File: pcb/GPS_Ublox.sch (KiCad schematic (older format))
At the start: 0 parts

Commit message: Add MTX2 circuit and add a sheet for power supply/regulation
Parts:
- added IC?: u-blox_CAM-M8Q, symbol u-blox_CAM-M8Q
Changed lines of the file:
@@
 LIBS:max-7q
 LIBS:ms5611-01ba03
-LIBS:quarter_wave_ant
 LIBS:resistor
 LIBS:rfm69w
-LIBS:sma
 LIBS:stm32f405vgt
 LIBS:swd
@@
 LIBS:stm32f072cbt6
 LIBS:jsta
+LIBS:sma
+LIBS:cga0402mlc-12g
 LIBS:woodchuck-cache
 EELAYER 25 0
@@
 $Descr A4 11693 8268
 encoding utf-8
-Sheet 1 6
+Sheet 2 7
 Title ""
 Date ""
@@
 Comment4 ""
 $EndDescr
+$Comp
+L u-blox_CAM-M8Q IC?
+U 1 1 565D0659
+P 5350 2900
+F 0 "IC?" H 4900 3450 60  0000 C CNN
+F 1 "u-blox_CAM-M8Q" H 5250 1400 60  0000 C CNN
+F 2 "" H 5550 2000 60  0000 C CNN
+F 3 "" H 5550 2000 60  0000 C CNN
+	1    5350 2900
+	1    0    0    -1
+$EndComp
 $EndSCHEMATC

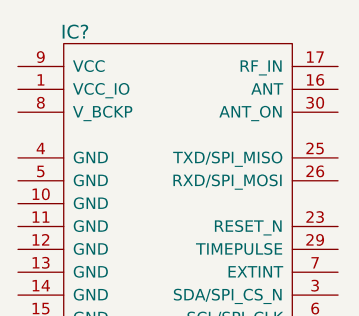
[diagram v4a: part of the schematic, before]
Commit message: Modify pin assignments of MCU
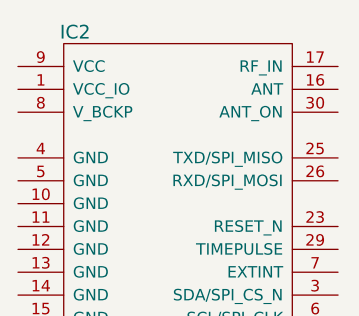
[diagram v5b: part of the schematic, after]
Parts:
- gave numbers to parts that had none: 1
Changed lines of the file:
@@
 $EndDescr
 $Comp
-L u-blox_CAM-M8Q IC?
+L u-blox_CAM-M8Q IC2
 U 1 1 565D0659
 P 5350 2900
-F 0 "IC?" H 4900 3450 60  0000 C CNN
+F 0 "IC2" H 4900 3450 60  0000 C CNN
 F 1 "u-blox_CAM-M8Q" H 5250 1400 60  0000 C CNN
 F 2 "" H 5550 2000 60  0000 C CNN

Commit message: Begin routing GPS
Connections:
- net +3V3: now reaches IC2.1 (VCC_IO)
- net +3V3: now also IC2.9 (VCC)
- net GND: now reaches IC2.10 (GND)
- net GND: now also IC2.11 (GND), IC2.12 (GND), IC2.13 (GND), IC2.14 (GND), IC2.15 (GND), IC2.18 (GND), IC2.19 (GND), IC2.21 (GND), IC2.22 (GND), IC2.27 (GND), IC2.31 (GND), IC2.4 (GND), IC2.5 (GND)
- no-connect marks 0 -> 1
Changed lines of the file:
@@
 	1    0    0    -1
 $EndComp
+$Comp
+L GND #PWR?
+U 1 1 56AAB217
+P 4550 4300
+F 0 "#PWR?" H 4550 4050 50  0001 C CNN
+F 1 "GND" H 4550 4150 50  0000 C CNN
+F 2 "" H 4550 4300 60  0000 C CNN
+F 3 "" H 4550 4300 60  0000 C CNN
+	1    4550 4300
+	1    0    0    -1
+$EndComp
+Wire Wire Line
+	4650 4200 4550 4200
+Wire Wire Line
+	4550 2900 4550 4300
+Wire Wire Line
+	4650 2900 4550 2900
+Connection ~ 4550 4200
+Wire Wire Line
+	4650 3000 4550 3000
+Connection ~ 4550 3000
+Wire Wire Line
+	4650 3100 4550 3100
+Connection ~ 4550 3100
+Wire Wire Line
+	4650 3200 4550 3200
+Connection ~ 4550 3200
+Wire Wire Line
+	4650 3300 4550 3300
+Connection ~ 4550 3300
+Wire Wire Line
+	4650 3400 4550 3400
+Connection ~ 4550 3400
+Wire Wire Line
+	4650 3500 4550 3500
+Connection ~ 4550 3500
+Wire Wire Line
+	4650 3600 4550 3600
+Connection ~ 4550 3600
+Wire Wire Line
+	4650 3700 4550 3700
+Connection ~ 4550 3700
+Wire Wire Line
+	4650 3800 4550 3800
+Connection ~ 4550 3800
+Wire Wire Line
+	4650 3900 4550 3900
+Connection ~ 4550 3900
+Wire Wire Line
+	4650 4000 4550 4000
+Connection ~ 4550 4000
+Wire Wire Line
+	4650 4100 4550 4100
+Connection ~ 4550 4100
+$Comp
+L +3.3V #PWR?
+U 1 1 56AAB35F
+P 4550 2400
+F 0 "#PWR?" H 4550 2250 50  0001 C CNN
+F 1 "+3.3V" H 4550 2540 50  0000 C CNN
+F 2 "" H 4550 2400 60  0000 C CNN
+F 3 "" H 4550 2400 60  0000 C CNN
+	1    4550 2400
+	1    0    0    -1
+$EndComp
+Wire Wire Line
+	4550 2400 4550 2600
+Wire Wire Line
+	4550 2500 4650 2500
+Wire Wire Line
+	4550 2600 4650 2600
+Connection ~ 4550 2500
+NoConn ~ 4650 2700
+Text HLabel 7650 2800 0    60   Input ~ 0
+GPS_FROM_MCU
+Text HLabel 7700 3000 0    60   Output ~ 0
+GPS_TO_MCU
 $EndSCHEMATC

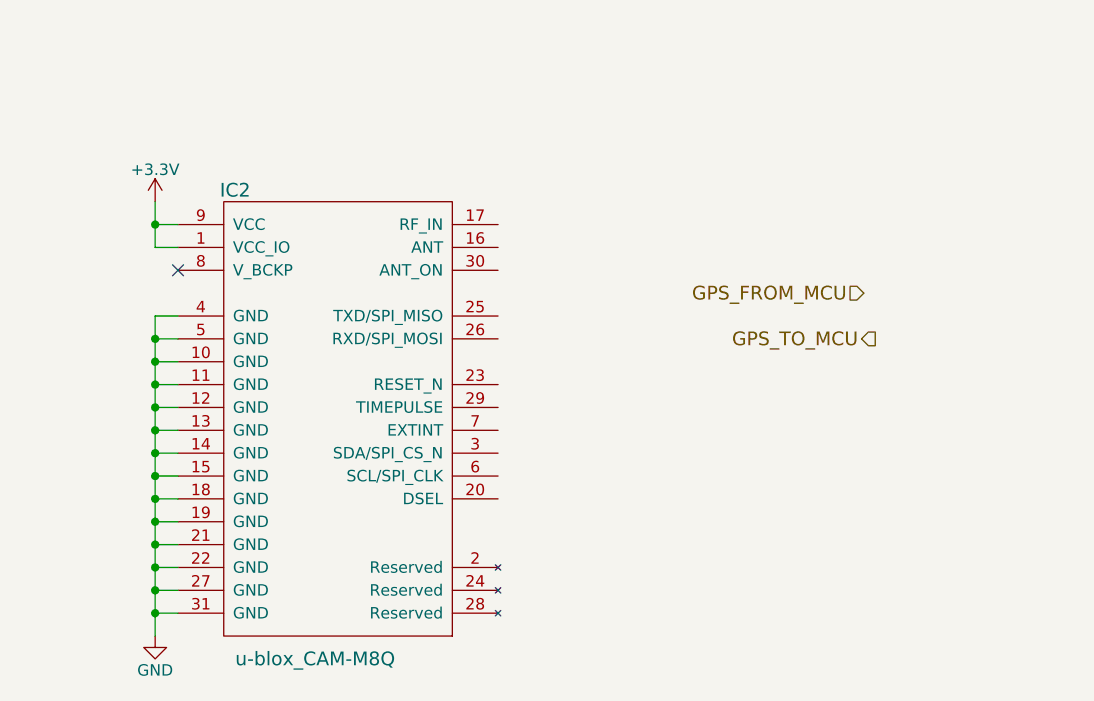
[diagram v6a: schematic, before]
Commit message: Finished schematics for GPS. TODO: check DSEL, and that RX TX are connected correctly. Make sure capacitor and resistor values are ok.
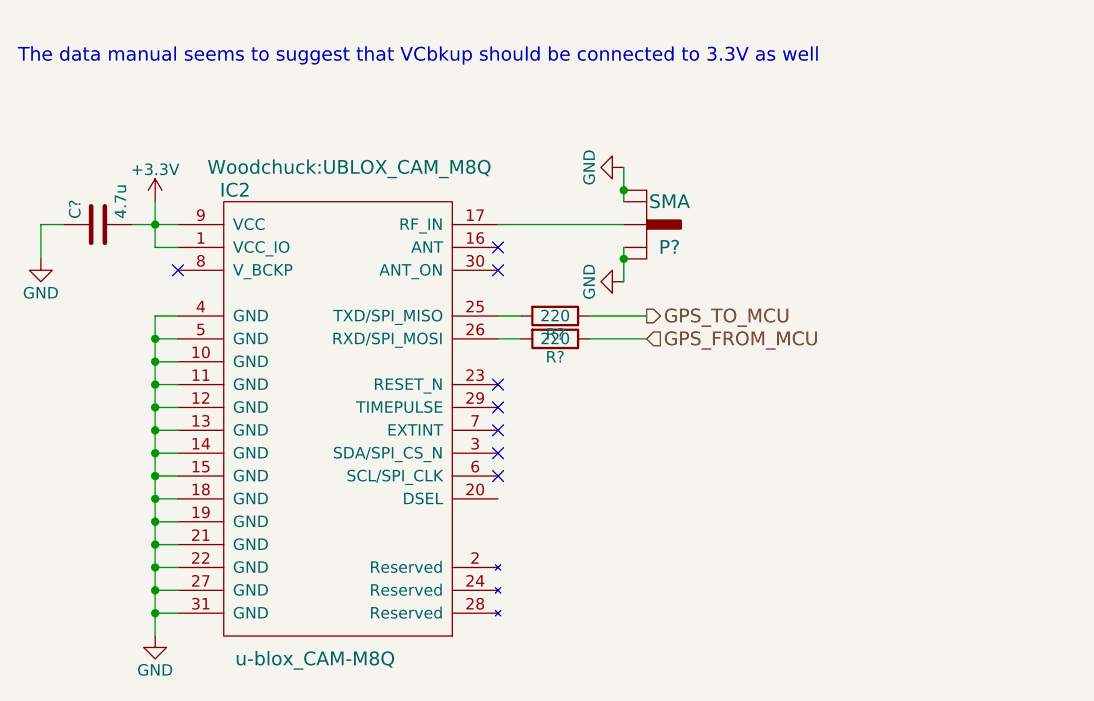
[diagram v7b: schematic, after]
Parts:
- added C?: 4.7u, symbol C
- added P?: SMA, symbol SMA
- added R? (x2): 220, symbol R
- IC2: footprint (none) -> Woodchuck:UBLOX_CAM_M8Q
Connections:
- net +3V3: now also C?.2
- net GND: now also C?.1, P?.2 (GND), P?.3 (GND), P?.4 (GND), P?.5 (GND)
- net GPS_FROM_MCU: now also R?.1
- net GPS_TO_MCU: now also R?.1
- net at IC2.17 (RF_IN): now also P?.1 (RF)
- net at IC2.25 (TXD/SPI_MISO): now also R?.2
- net at IC2.26 (RXD/SPI_MOSI): now also R?.2
- no-connect marks 1 -> 8
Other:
- note added: "The data manual seems to suggest that VCbkup should be connected to 3.3V as well"
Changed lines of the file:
@@
 F 0 "IC2" H 4900 3450 60  0000 C CNN
 F 1 "u-blox_CAM-M8Q" H 5250 1400 60  0000 C CNN
-F 2 "" H 5550 2000 60  0000 C CNN
+F 2 "Woodchuck:UBLOX_CAM_M8Q" H 5400 3550 60  0000 C CNN
 F 3 "" H 5550 2000 60  0000 C CNN
 	1    5350 2900
@@
 	4550 2400 4550 2600
 Wire Wire Line
-	4550 2500 4650 2500
+	4450 2500 4650 2500
 Wire Wire Line
 	4550 2600 4650 2600
 Connection ~ 4550 2500
 NoConn ~ 4650 2700
-Text HLabel 7650 2800 0    60   Input ~ 0
+Text HLabel 6700 3000 2    60   Input ~ 0
 GPS_FROM_MCU
-Text HLabel 7700 3000 0    60   Output ~ 0
+Text HLabel 6700 2900 2    60   Output ~ 0
 GPS_TO_MCU
+Text Notes 3950 1800 0    60   ~ 0
+The data manual seems to suggest that VCbkup should be connected to 3.3V as well
+$Comp
+L C C?
+U 1 1 56ACB00C
+P 4300 2500
+F 0 "C?" H 4325 2600 50  0000 L CNN
+F 1 "4.7u" H 4325 2400 50  0000 L CNN
+F 2 "" H 4338 2350 30  0000 C CNN
+F 3 "" H 4300 2500 60  0000 C CNN
+	1    4300 2500
+	0    -1   -1   0
+$EndComp
+Wire Wire Line
+	4150 2500 4050 2500
+Wire Wire Line
+	4050 2500 4050 2650
+$Comp
+L GND #PWR?
+U 1 1 56ACB0DE
+P 4050 2650
+F 0 "#PWR?" H 4050 2400 50  0001 C CNN
+F 1 "GND" H 4050 2500 50  0000 C CNN
+F 2 "" H 4050 2650 60  0000 C CNN
+F 3 "" H 4050 2650 60  0000 C CNN
+	1    4050 2650
+	1    0    0    -1
+$EndComp
+$Comp
+L SMA P?
+U 1 1 56ACB5C4
+P 6700 2500
+F 0 "P?" H 6800 2400 60  0000 C CNN
+F 1 "SMA" H 6800 2600 60  0000 C CNN
+F 2 "" H 6700 2500 60  0000 C CNN
+F 3 "" H 6700 2500 60  0000 C CNN
+	1    6700 2500
+	1    0    0    -1
+$EndComp
+Wire Wire Line
+	6600 2600 6600 2750
+Connection ~ 6600 2650
+Wire Wire Line
+	6600 2250 6600 2400
+Connection ~ 6600 2350
+Wire Wire Line
+	6600 2500 6050 2500
+$Comp
+L GND #PWR?
+U 1 1 56ACB7D0
+P 6600 2250
+F 0 "#PWR?" H 6600 2000 50  0001 C CNN
+F 1 "GND" H 6600 2100 50  0000 C CNN
+F 2 "" H 6600 2250 60  0000 C CNN
+F 3 "" H 6600 2250 60  0000 C CNN
+	1    6600 2250
+	0    1    1    0
+$EndComp
+$Comp
+L GND #PWR?
+U 1 1 56ACB7EA
+P 6600 2750
+F 0 "#PWR?" H 6600 2500 50  0001 C CNN
+F 1 "GND" H 6600 2600 50  0000 C CNN
+F 2 "" H 6600 2750 60  0000 C CNN
+F 3 "" H 6600 2750 60  0000 C CNN
+	1    6600 2750
+	0    1    1    0
+$EndComp
+NoConn ~ 6050 2600
+NoConn ~ 6050 2700
+$Comp
+L R R?
+U 1 1 56ACBA41
+P 6300 3000
+F 0 "R?" V 6380 3000 50  0000 C CNN
+F 1 "220" V 6300 3000 50  0000 C CNN
+F 2 "" V 6230 3000 30  0000 C CNN
+F 3 "" H 6300 3000 30  0000 C CNN
+	1    6300 3000
+	0    1    1    0
+$EndComp
+$Comp
+L R R?
+U 1 1 56ACBA86
+P 6300 2900
+F 0 "R?" V 6380 2900 50  0000 C CNN
+F 1 "220" V 6300 2900 50  0000 C CNN
+F 2 "" V 6230 2900 30  0000 C CNN
+F 3 "" H 6300 2900 30  0000 C CNN
+	1    6300 2900
+	0    1    1    0
+$EndComp
+Wire Wire Line
+	6150 2900 6050 2900
+Wire Wire Line
+	6050 3000 6150 3000
+Wire Wire Line
+	6450 2900 6700 2900
+Wire Wire Line
+	6450 3000 6700 3000
+NoConn ~ 6050 3600
+NoConn ~ 6050 3500
+NoConn ~ 6050 3400
+NoConn ~ 6050 3300
+NoConn ~ 6050 3200
 $EndSCHEMATC

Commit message: Change decoupling cap to 100nF (like other projects) and connect V_BCKP to VCC
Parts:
- C?: value 4.7u -> 100n; footprint (none) -> Woodchuck:C0603; Digikey (none) -> Value; Farnell (none) -> 9406140; Fieldname (none) -> Value
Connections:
- net +3V3: now also IC2.8 (V_BCKP)
- no-connect marks 8 -> 7
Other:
- note added: "-How are we interfacing to the MCU? DSEL may have to be grounded\n-Embedded antenna?"
- note removed: "The data manual seems to suggest that VCbkup should be connected to 3.3V as well"
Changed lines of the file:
@@
 $EndComp
 Wire Wire Line
-	4550 2400 4550 2600
+	4550 2400 4550 2700
 Wire Wire Line
 	4450 2500 4650 2500
@@
 	4550 2600 4650 2600
 Connection ~ 4550 2500
-NoConn ~ 4650 2700
 Text HLabel 6700 3000 2    60   Input ~ 0
 GPS_FROM_MCU
@@
 GPS_TO_MCU
 Text Notes 3950 1800 0    60   ~ 0
-The data manual seems to suggest that VCbkup should be connected to 3.3V as well
+-How are we interfacing to the MCU? DSEL may have to be grounded\n-Embedded antenna?
 $Comp
 L C C?
@@
 P 4300 2500
 F 0 "C?" H 4325 2600 50  0000 L CNN
-F 1 "4.7u" H 4325 2400 50  0000 L CNN
-F 2 "" H 4338 2350 30  0000 C CNN
+F 1 "100n" H 4325 2400 50  0000 L CNN
+F 2 "Woodchuck:C0603" H 4338 2350 30  0001 C CNN
 F 3 "" H 4300 2500 60  0000 C CNN
+F 4 "Value" H 4300 2500 60  0001 C CNN "Digikey"
+F 5 "9406140" H 4300 2500 60  0001 C CNN "Farnell"
+F 6 "Value" H 4300 2500 60  0001 C CNN "Fieldname"
 	1    4300 2500
 	0    -1   -1   0
@@
 NoConn ~ 6050 3300
 NoConn ~ 6050 3200
+Wire Wire Line
+	4550 2700 4650 2700
+Connection ~ 4550 2600
 $EndSCHEMATC
